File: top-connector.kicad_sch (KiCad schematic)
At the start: 6 parts, among them J1 Plug_Hirose_DF40_2x50_DF40C-1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, Q2 DMG1012T-7

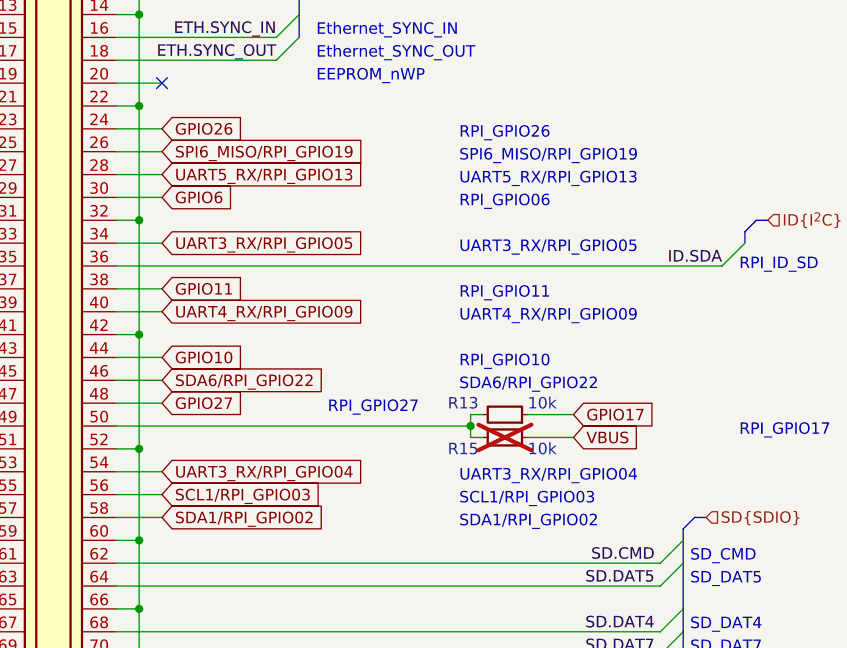
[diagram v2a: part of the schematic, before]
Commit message: [#60587] Update UART3 and UART5 nets
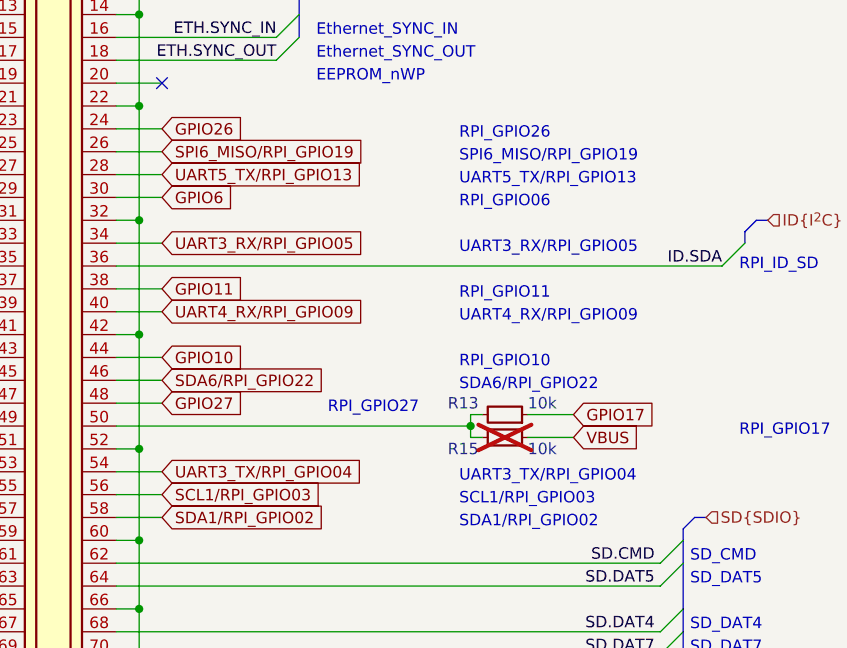
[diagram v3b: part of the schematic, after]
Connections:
- net UART3_RX/RPI_GPIO04 renamed UART3_TX/RPI_GPIO04
- net UART5_RX/RPI_GPIO13 renamed UART5_TX/RPI_GPIO13
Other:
- note added: "UART3_TX/RPI_GPIO04"
- note added: "UART5_TX/RPI_GPIO13"
- note removed: "UART3_RX/RPI_GPIO04"
- note removed: "UART5_RX/RPI_GPIO13"
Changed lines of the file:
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@@
     (effects (font (size 1.27 1.27)) (justify right bottom))
   )
-  (text "UART5_RX/RPI_GPIO13" (at 254 111.76 0)
+  (text "UART5_TX/RPI_GPIO13" (at 254 111.76 0)
     (effects (font (size 1.27 1.27)) (justify left bottom))
   )
@@
     (effects (font (size 1.27 1.27)) (justify right bottom))
   )
-  (text "UART3_RX/RPI_GPIO04" (at 254 144.78 0)
+  (text "UART3_TX/RPI_GPIO04" (at 254 144.78 0)
     (effects (font (size 1.27 1.27)) (justify left bottom))
   )
@@
     )
   )
-  (global_label "UART3_RX{slash}RPI_GPIO04" (shape input) (at 220.98 143.51 0) (fields_autoplaced)
-    (effects (font (size 1.27 1.27)) (justify left))
-    (property "Intersheetrefs" "${INTERSHEET_REFS}" (at 245.0436 143.4306 0)
+  (global_label "UART3_TX{slash}RPI_GPIO04" (shape input) (at 220.98 143.51 0) (fields_autoplaced)
+    (effects (font (size 1.27 1.27)) (justify left))
+    (property "Intersheetrefs" "${INTERSHEET_REFS}" (at 245.3133 143.51 0)
       (effects (font (size 1.27 1.27)) (justify left))
     )
@@
     )
   )
-  (global_label "UART5_RX{slash}RPI_GPIO13" (shape input) (at 220.98 110.49 0) (fields_autoplaced)
-    (effects (font (size 1.27 1.27)) (justify left))
-    (property "Intersheetrefs" "${INTERSHEET_REFS}" (at 245.0436 110.4106 0)
-      (effects (font (size 1.27 1.27)) (justify left))
-    )
+  (global_label "UART5_TX{slash}RPI_GPIO13" (shape input) (at 220.98 110.49 0) (fields_autoplaced)
+    (effects (font (size 1.27 1.27)) (justify left))
+    (property "Intersheetrefs" "${INTERSHEET_REFS}" (at 245.3133 110.49 0)
+      (effects (font (size 1.27 1.27)) (justify left))
+    )
